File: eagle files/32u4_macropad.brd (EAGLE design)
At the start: 75.2 x 98.6 mm, 91 parts, among them J1 TYPE-C-31-M-12, Q1 16MHz, SW2 SWITCH-SMD-EVP-BB2A9B00

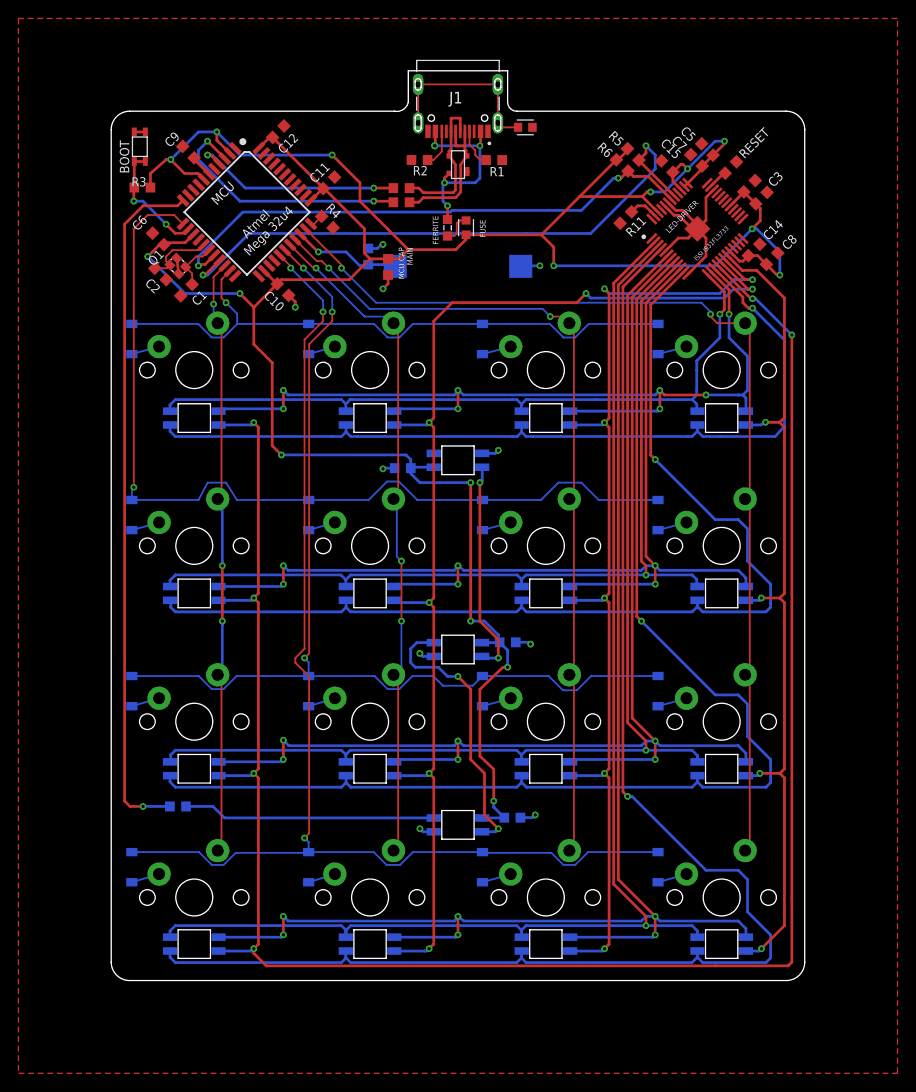
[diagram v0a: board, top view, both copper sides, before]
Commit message: Small routing fixes, added credits in sch and brd
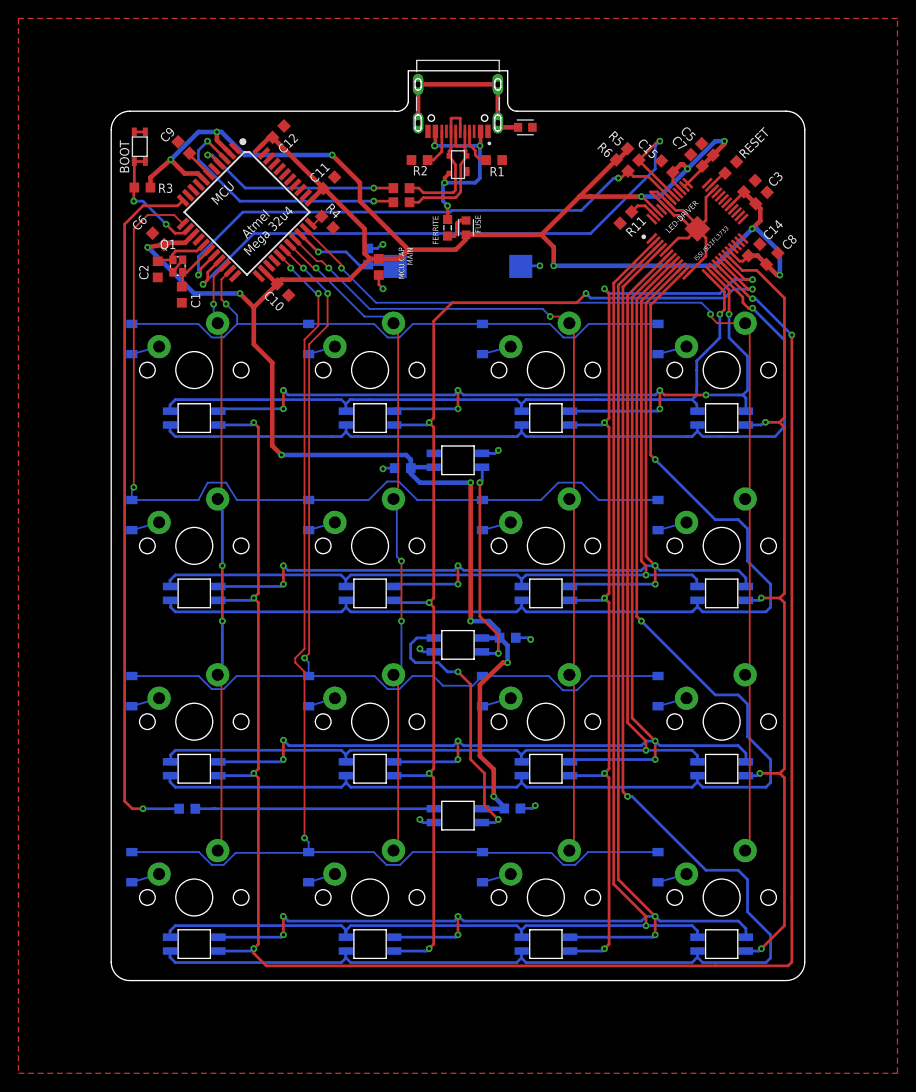
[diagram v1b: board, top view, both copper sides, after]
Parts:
- moved R12 1.03 mm to (18.3, 28.7)
- moved C13 1.00 mm to (39.0, 87.4)
- moved C21 1.00 mm to (53.5, 28.7)
- moved UGLOW1 1.00 mm to (47.6, 27.9)
- moved C1 0.71 mm to (17.7, 84.4), turned to 90 degrees
- moved C9 0.71 mm to (17.9, 100.3)
- moved C2 0.59 mm to (15.1, 87.1), turned to 90 degrees
- moved C20 0.50 mm to (53.0, 47.2)
- moved UGLOW2 0.50 mm to (47.6, 46.4)
- turned Q1 to 90 degrees
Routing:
- net GND: track 45.9 -> 49.1 mm, vias 10 -> 9
- net SDA: track 66.7 -> 69.4 mm
- net SCL: track 59.6 -> 61.3 mm
- net N$7: track 27.4 -> 25.8 mm
- net N$5: track 7.49 -> 6.08 mm
- net VCC: track 304.6 -> 303.5 mm
- net UNDGLOW: track 75.1 -> 76.2 mm
- net N$20: track 2.45 -> 3.16 mm
- net R3SWTCH: track 129.3 -> 128.7 mm
- net N$39: track 30.2 -> 29.7 mm
- net N$25: track 23.4 -> 22.9 mm
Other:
- board text added: "KeyboardAtelier@Discord"
- board text added: "Stefano Nicolis Thiird@Github"
- board text added: "UNDERGLOW SIG"

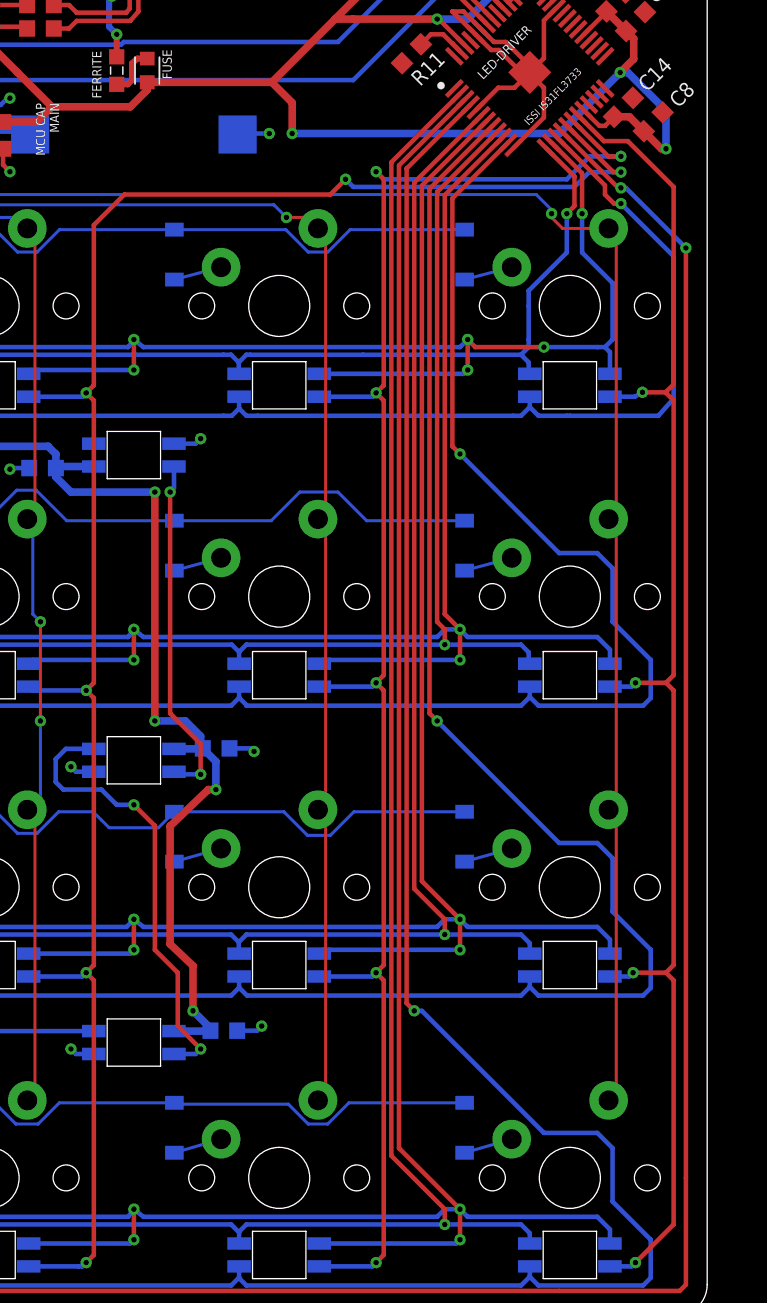
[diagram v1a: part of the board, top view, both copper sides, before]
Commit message: Led driver connections to leds fixed in sch and brd
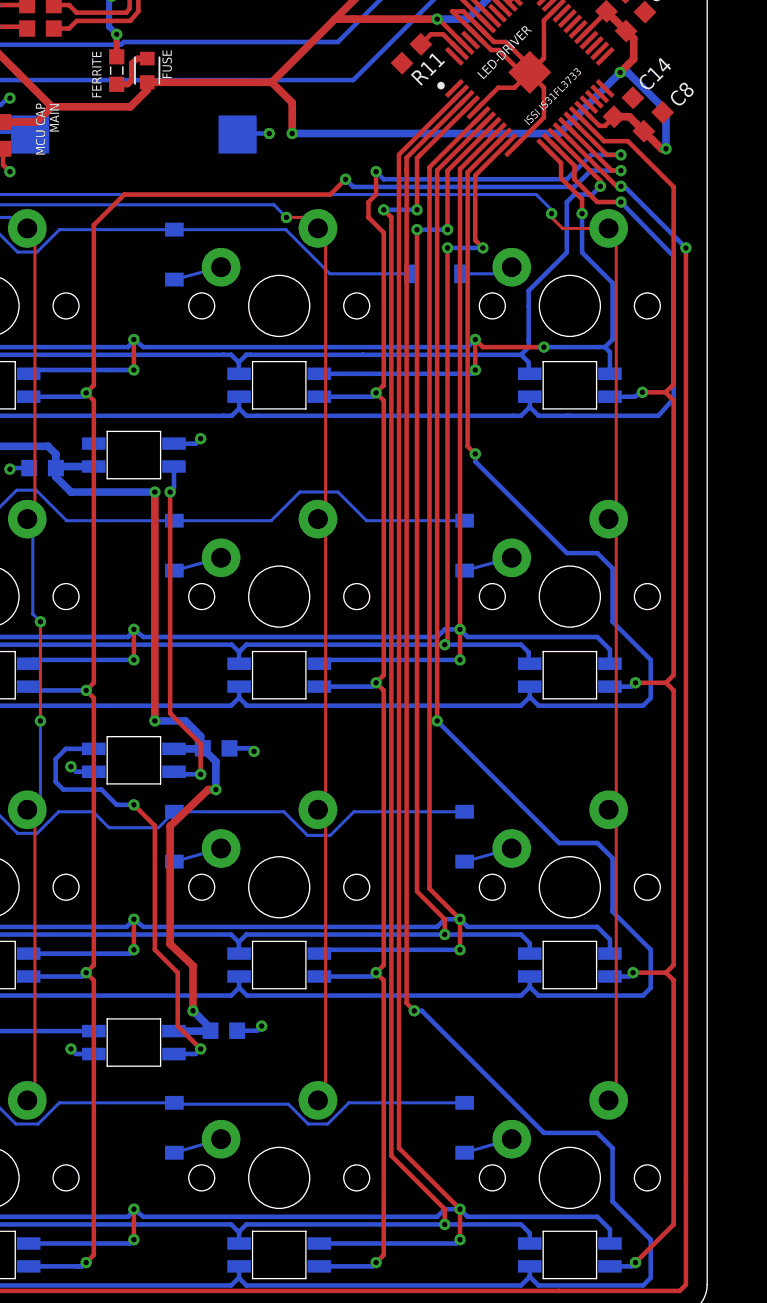
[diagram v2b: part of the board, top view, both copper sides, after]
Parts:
- moved D3 2.25 mm to (67.4, 78.3), turned to 0 degrees
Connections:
- net R0BLUE: now also DRIVER.15; no longer DRIVER.13
- net R0GREEN: now also DRIVER.13; no longer DRIVER.14
- net R0RED: now also DRIVER.14; no longer DRIVER.15
- net R1BLUE: now also DRIVER.11; no longer DRIVER.9
- net R1GREEN: now also DRIVER.9; no longer DRIVER.10
- net R1RED: now also DRIVER.10; no longer DRIVER.11
- net R2BLUE: now also DRIVER.8; no longer DRIVER.6
- net R2GREEN: now also DRIVER.6; no longer DRIVER.7
- net R2RED: now also DRIVER.7; no longer DRIVER.8
- net R3BLUE: now also DRIVER.4; no longer DRIVER.2
- net R3GREEN: now also DRIVER.2; no longer DRIVER.3
- net R3RED: now also DRIVER.3; no longer DRIVER.4
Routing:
- net R0SWTCH: track 67.5 -> 64.0 mm
- net R0BLUE: track 77.1 -> 79.6 mm
- net R3BLUE: track 140.2 -> 141.6 mm, vias 1 -> 3
- net R1BLUE: track 96.8 -> 97.7 mm, vias 1 -> 3
- net R1RED: track 114.5 -> 113.6 mm
- net R1GREEN: track 116.2 -> 115.5 mm
- net R2BLUE: track 117.7 -> 118.3 mm, vias 1 -> 3

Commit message: brd minor fixes
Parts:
- moved C1 2.16 mm to (15.7, 85.1), turned to 45 degrees
- moved C2 1.05 mm to (14.4, 86.4), turned to 45 degrees
- moved C10 0.71 mm to (29.2, 84.4)
- moved C6 0.50 mm to (15.2, 90.9)
- moved Q1 0.42 mm to (17.2, 87.9), turned to 45 degrees
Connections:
- net R1SWTCH: now also MCU.26; no longer MCU.12
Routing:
- net R1SWTCH: track 98.2 -> 91.3 mm, vias 1 -> 3
- net SCL: track 61.3 -> 62.4 mm
- net R2GREEN: track 136.9 -> 135.9 mm
- net R1GREEN: track 115.5 -> 114.5 mm
- net N$5: track 6.08 -> 7.07 mm
- net N$39: track 29.7 -> 30.4 mm
- net GND: track 49.1 -> 48.5 mm
- net N$21: track 5.55 -> 6.14 mm
- net N$15: track 23.3 -> 23.8 mm
- net R0GREEN: track 98.3 -> 98.8 mm
- net C0SWTCH: vias 3 -> 2

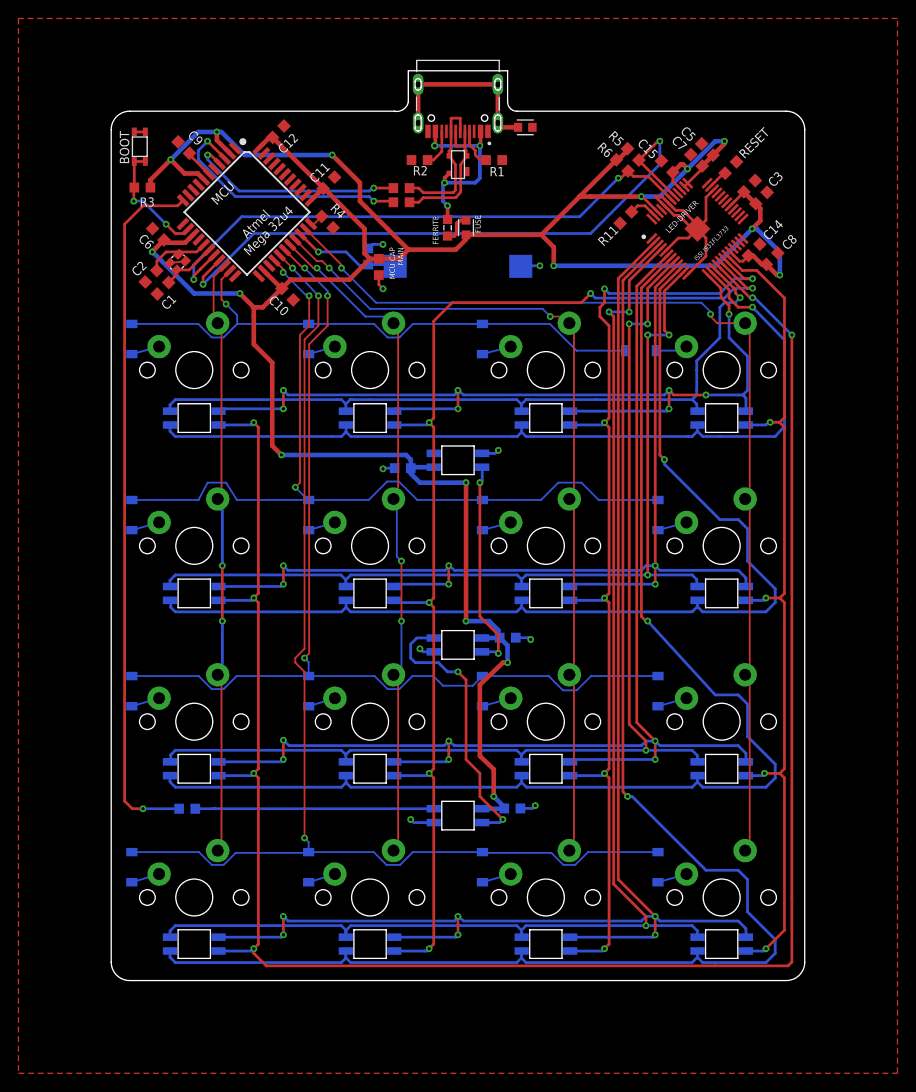
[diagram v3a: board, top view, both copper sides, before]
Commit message: Enlarged pcb on top for case matching, re routed to accomodate this change
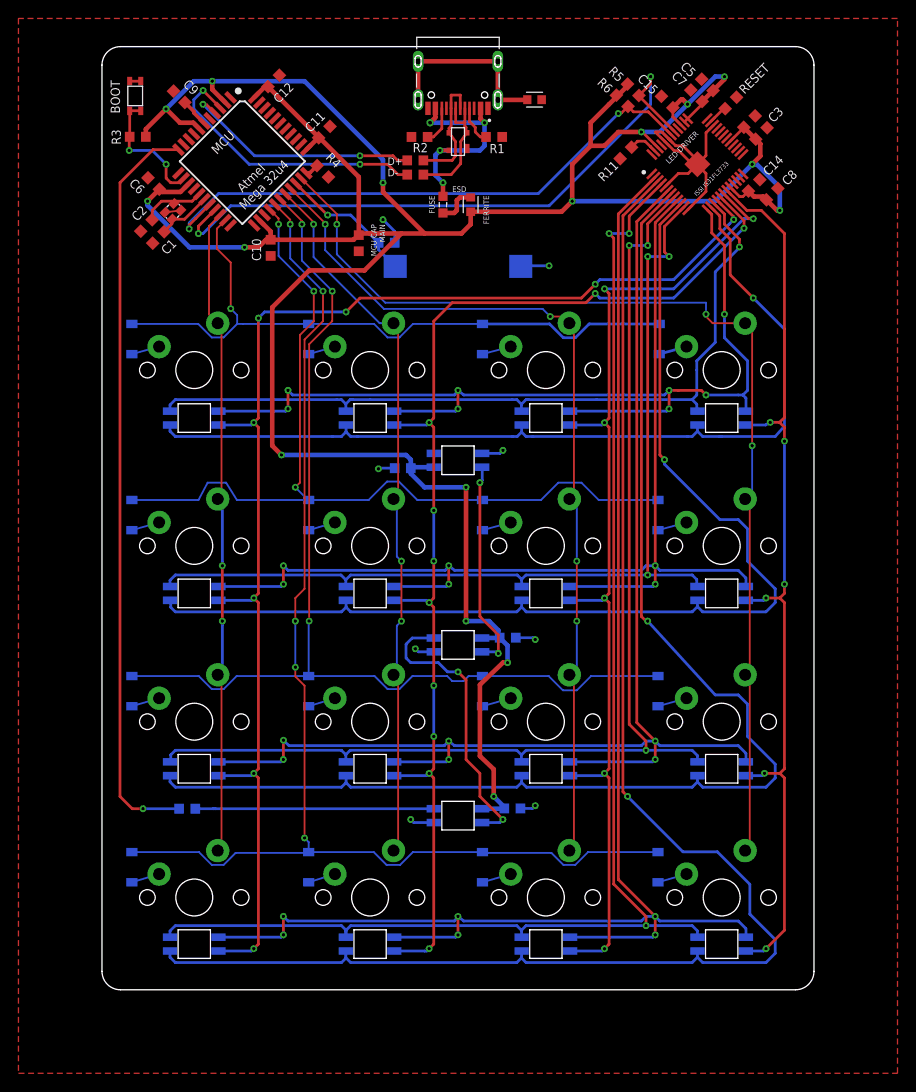
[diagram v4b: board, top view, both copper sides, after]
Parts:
- moved C14 7.00 mm to (79.7, 96.2)
- moved C15 7.00 mm to (70.3, 105.2)
- moved C3 7.00 mm to (80.5, 101.8)
- moved C4 7.00 mm to (79.2, 103.1)
- moved C5 7.00 mm to (74.6, 107.1)
- moved C7 7.00 mm to (73.5, 105.9)
- moved C8 7.00 mm to (81.7, 95.3)
- moved DRIVER 7.00 mm to (73.6, 98.5)
- moved R11 7.00 mm to (65.8, 99.7)
- moved R5 7.00 mm to (66.6, 106.6)
- moved R6 7.00 mm to (65.4, 105.4)
- moved RESET 7.00 mm to (77.2, 105.1)
- moved C1 5.52 mm to (15.2, 90.6)
- moved C11 5.52 mm to (33.1, 102.0)
- moved C12 5.52 mm to (27.7, 107.5)
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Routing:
- net C0RGB: track 220.6 -> 144.3 mm, vias 6 -> 8
- net VCC: track 303.6 -> 325.4 mm
- net R0SWTCH: track 64.0 -> 73.4 mm
- net R2GREEN: track 135.9 -> 142.9 mm
- net C3RGB: track 94.3 -> 101.3 mm, vias 4 -> 6
- net R3GREEN: track 158.3 -> 165.3 mm
- net R3BLUE: track 141.5 -> 148.5 mm
- net R2RED: track 135.5 -> 142.5 mm
- net R2BLUE: track 118.3 -> 125.3 mm
- net R1RED: track 114.0 -> 121.0 mm
- net R1BLUE: track 97.6 -> 104.6 mm
- net R1GREEN: track 114.5 -> 121.5 mm
- net R0GREEN: track 98.8 -> 105.8 mm
- net R3RED: track 159.4 -> 166.2 mm
- net R0BLUE: track 79.6 -> 85.9 mm
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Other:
- board size 75.2 x 98.6 mm -> 77.2 x 102.2 mm
- board text added: "D+ D-"
- board text added: "ESD"

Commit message: Small board fixes
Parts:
- moved C16 1.12 mm to (38.9, 90.5)
- moved C20 1.00 mm to (54.0, 47.2)
- moved FERRITE_VCC 0.50 mm to (49.0, 93.6)
- moved FUSE 0.50 mm to (46.0, 93.6)
- moved R7 0.50 mm to (42.5, 98.9)
- moved R8 0.50 mm to (42.5, 97.4)
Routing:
- net R0BLUE: track 85.9 -> 89.0 mm
- net C1RGB: track 127.6 -> 129.8 mm
- net VBUS: track 23.5 -> 25.2 mm
- net GND: track 50.8 -> 49.2 mm
- net VCC: track 325.4 -> 326.9 mm
- net AUDIO: track 14.9 -> 16.1 mm
- net C1SWTCH: track 78.4 -> 77.4 mm
- net SDA: track 69.3 -> 70.2 mm
- net N$25: track 22.9 -> 23.8 mm
- net R0RED: track 98.6 -> 99.5 mm
- net C3SWTCH: track 116.6 -> 117.3 mm
- net N$6: track 31.1 -> 30.6 mm
- net N$15: track 26.3 -> 25.8 mm
- net D+: track 13.1 -> 13.6 mm
- net C2SWTCH: vias 4 -> 3

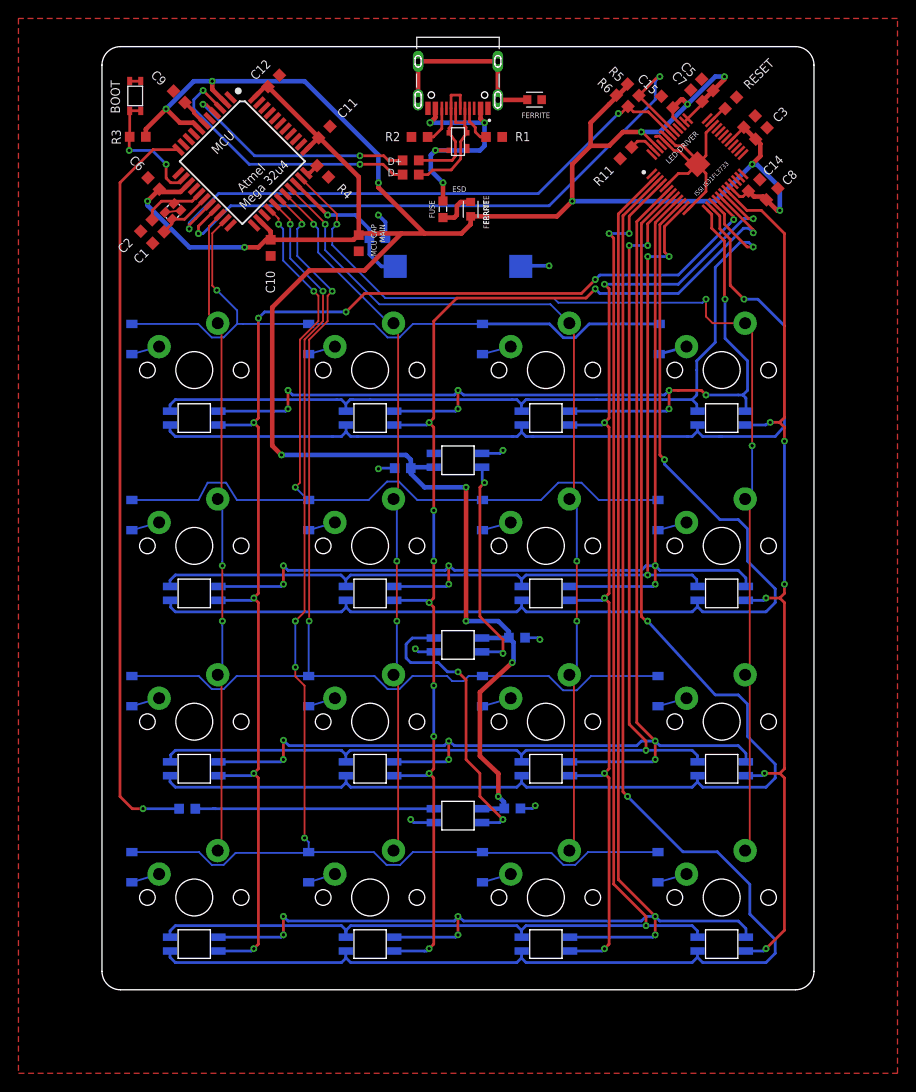
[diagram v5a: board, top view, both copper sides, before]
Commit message: Fixed xtal caps value and missing C4 name on brd
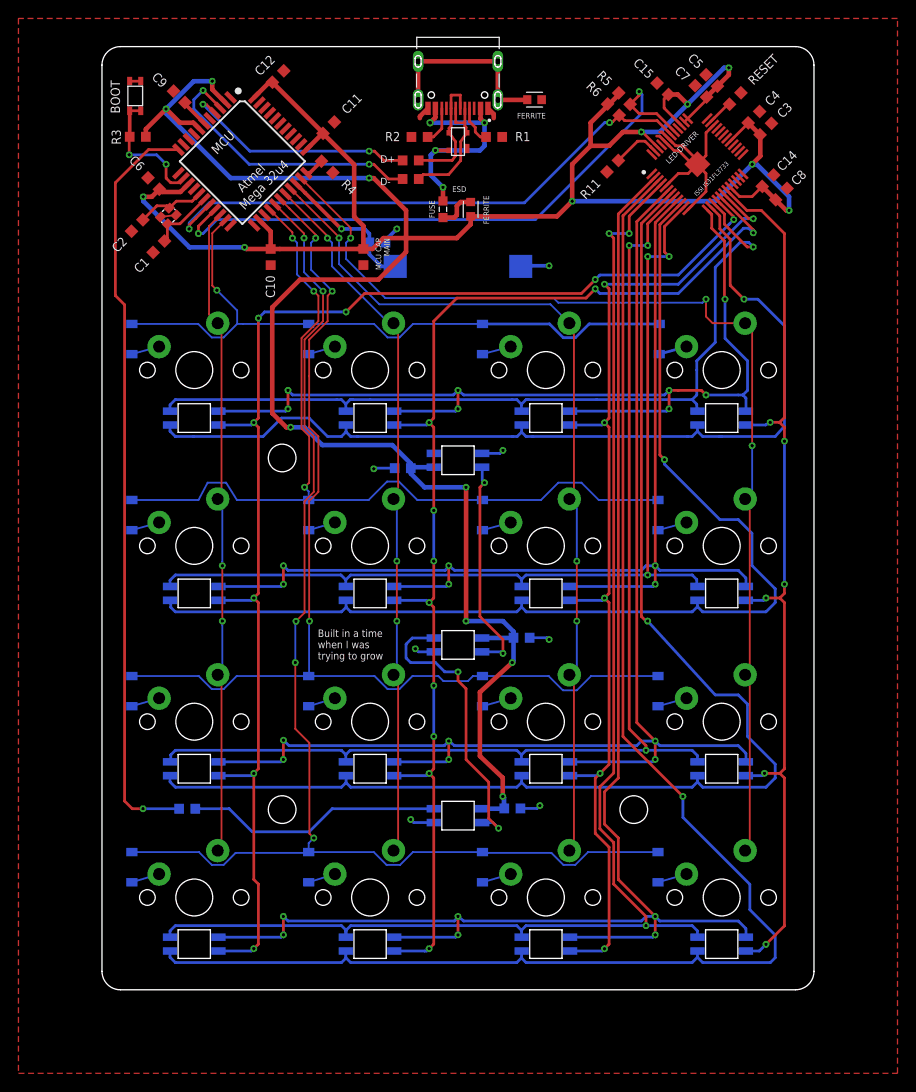
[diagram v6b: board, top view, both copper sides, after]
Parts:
- C1, C2: value 22uF -> 22pF
- moved R11 2.02 mm to (64.4, 98.3)
- moved C13 1.58 mm to (37.4, 88.5)
- moved C14 1.58 mm to (81.2, 96.7)
- moved C15 1.51 mm to (69.8, 106.7)
- moved R5 1.35 mm to (65.7, 105.6)
- moved R6 1.35 mm to (64.5, 104.4)
- moved C1 1.00 mm to (15.2, 89.6)
- moved C10 1.00 mm to (27.3, 88.4)
- moved C2 1.00 mm to (12.9, 91.9)
- moved C8 1.00 mm to (82.7, 95.3)
- moved Q1 0.71 mm to (16.2, 92.9)
- moved C11 0.67 mm to (33.6, 102.5)
- moved C3 0.67 mm to (81.0, 102.3)
- moved C4 0.67 mm to (79.7, 103.6)
- moved C5 0.67 mm to (75.1, 107.6)
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- renumbered SK6812MINI-E to UGLOW3
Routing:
- net VCC: track 326.9 -> 339.6 mm
- net GND: track 49.2 -> 52.4 mm
- net SDA: track 70.2 -> 67.1 mm
- net N$7: track 25.8 -> 27.9 mm
- net N$10: track 3.27 -> 5.29 mm
- net R3RED: track 166.2 -> 164.3 mm
- net R0RED: track 99.5 -> 101.2 mm
- net R3SWTCH: track 134.6 -> 135.9 mm
- net R3GREEN: track 165.3 -> 166.5 mm
- net R3BLUE: track 148.5 -> 149.8 mm
- net N$21: track 6.14 -> 7.12 mm
- net R2SWTCH: track 116.6 -> 117.4 mm
- net SCL: track 63.0 -> 62.2 mm
- net UNDGLOW: track 81.3 -> 82.0 mm
- net N$26: track 2.19 -> 2.87 mm
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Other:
- board text added: "Built in a time when I was trying to grow"
